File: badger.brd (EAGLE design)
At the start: 100 x 80 mm, 6 parts, among them U1 NCP1402

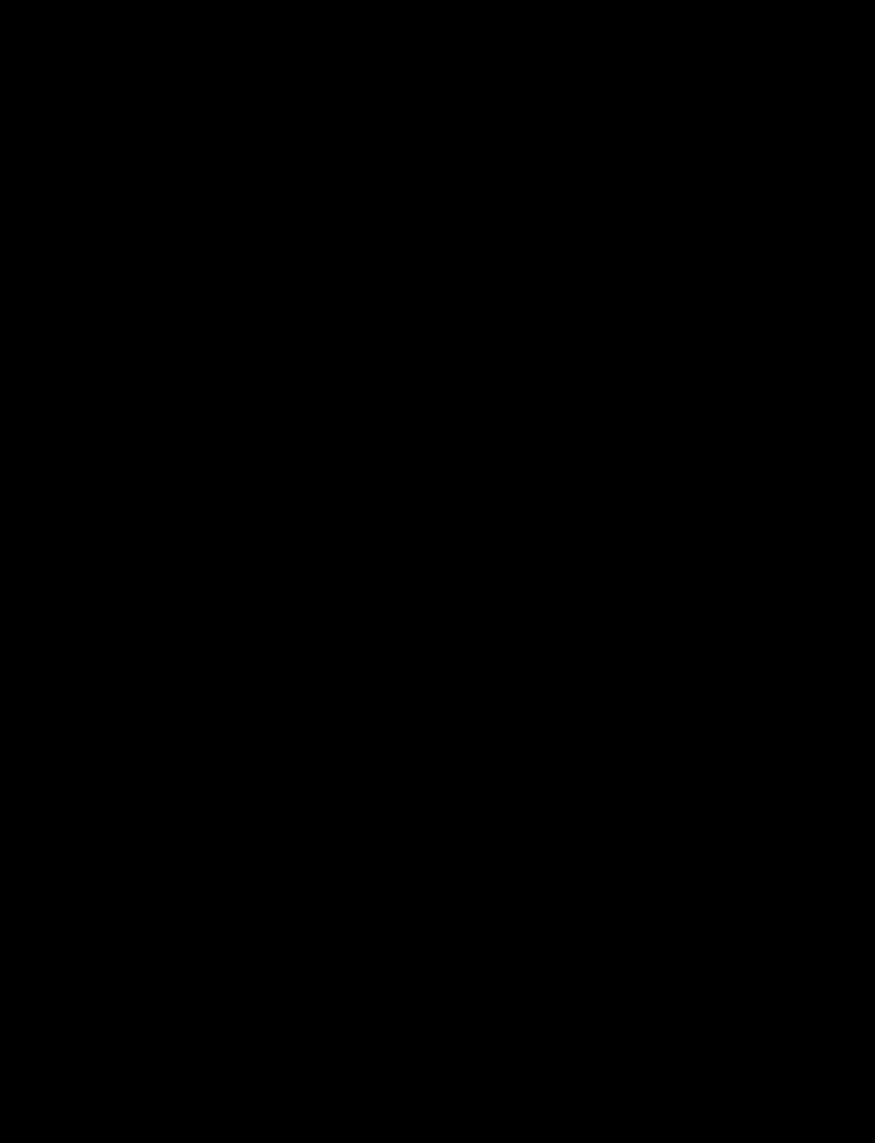
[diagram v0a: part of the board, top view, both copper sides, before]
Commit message: add esp8266 lib and add part
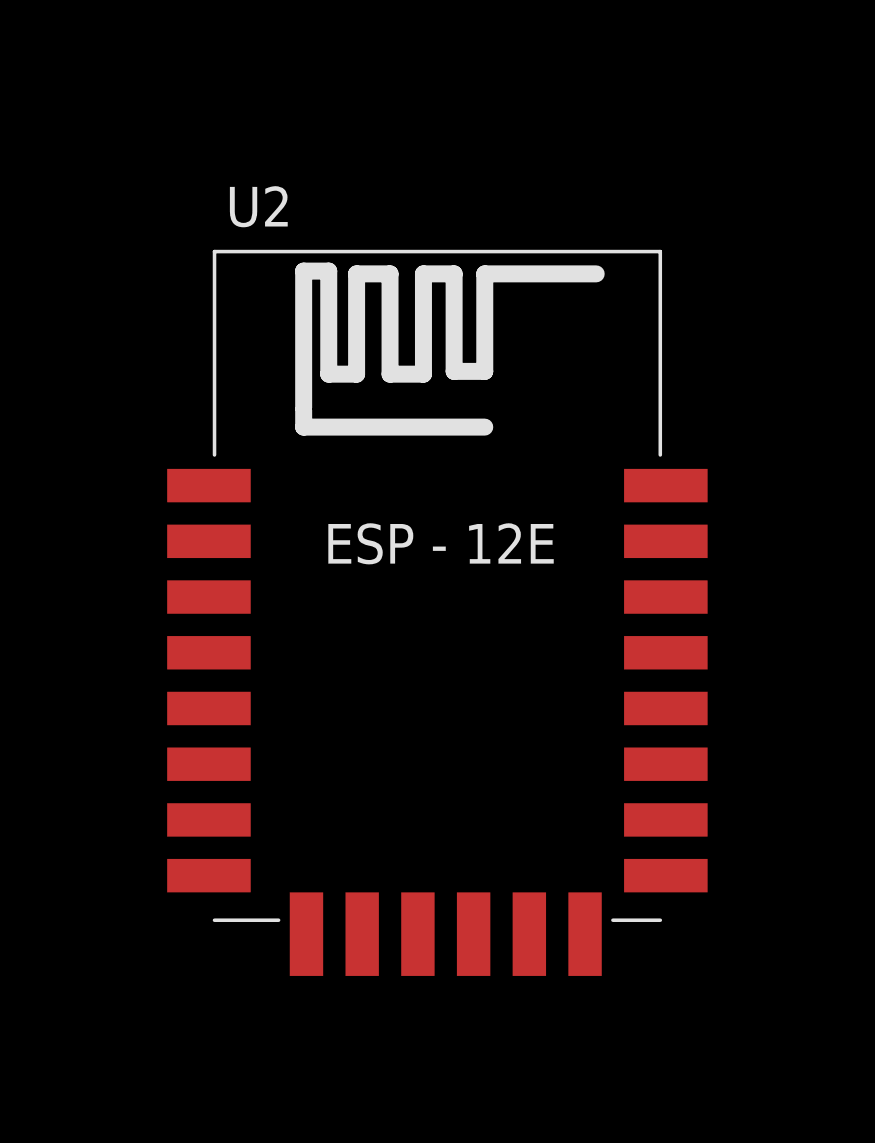
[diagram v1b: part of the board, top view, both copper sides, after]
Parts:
- added U2: (no value), esp8266modules:ESP12E-SMD
- C2: value 68uF -> 100uF
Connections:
- removed net VOUT: C2.A, D1.C, JP1.2, U1.1, U1.2
- new net VCC: C2.A, D1.C, JP1.2, U1.1, U1.2, U2.VCC
- net GND: now also U2.GND
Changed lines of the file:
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@@
 <elements>
 <element name="C1" library="SparkFun" package="EIA3216" value="10uF" x="39.37" y="41.91"/>
-<element name="C2" library="SparkFun" package="EIA3528" value="68uF" x="45.72" y="30.48"/>
+<element name="C2" library="SparkFun" package="EIA3528" value="100uF" x="45.72" y="30.48"/>
 <element name="D1" library="SparkFun" package="SMA-DIODE" value="MBRA140" x="45.72" y="41.91"/>
 <element name="JP1" library="SparkFun" package="1X03" value="" x="41.91" y="35.56"/>
 <element name="L1" library="SparkFun" package="CR54" value="47uH" x="45.72" y="24.13"/>
 <element name="U1" library="SparkFun" package="SOT23-5" value="NCP1402" x="38.1" y="36.83"/>
+<element name="U2" library="esp8266modules" package="ESP12E-SMD" value="" x="68.58" y="30.48"/>
 </elements>
 <signals>
@@
 <wire x1="43.57" y1="41.91" x2="37.15" y2="38.1301" width="0" layer="19" extent="1-1"/>
 </signal>
-<signal name="VOUT">
-<contactref element="U1" pad="1"/>
-<contactref element="U1" pad="2"/>
-<contactref element="D1" pad="C"/>
-<contactref element="C2" pad="A"/>
-<contactref element="JP1" pad="2"/>
-<wire x1="38.1" y1="35.5299" x2="37.15" y2="35.5299" width="0" layer="19" extent="1-1"/>
-<wire x1="44.45" y1="35.56" x2="38.1" y2="35.5299" width="0" layer="19" extent="1-1"/>
-<wire x1="47.37" y1="30.48" x2="44.45" y2="35.56" width="0" layer="19" extent="1-1"/>
-<wire x1="47.87" y1="41.91" x2="44.45" y2="35.56" width="0" layer="19" extent="1-1"/>
-</signal>
 <signal name="GND">
 <contactref element="C2" pad="C"/>
@@
 <contactref element="C1" pad="C"/>
 <contactref element="JP1" pad="1"/>
-<wire x1="41.91" y1="35.56" x2="44.07" y2="30.48" width="0" layer="19" extent="1-1"/>
-<wire x1="39.05" y1="38.1301" x2="41.91" y2="35.56" width="0" layer="19" extent="1-1"/>
+<contactref element="U2" pad="GND"/>
+<wire x1="41.91" y1="35.56" x2="39.05" y2="38.1301" width="0" layer="19" extent="1-1"/>
 <wire x1="37.97" y1="41.91" x2="39.05" y2="38.1301" width="0" layer="19" extent="1-1"/>
+<wire x1="44.07" y1="30.48" x2="41.91" y2="35.56" width="0" layer="19" extent="1-1"/>
+<wire x1="76.68" y1="22.28" x2="44.07" y2="30.48" width="0" layer="19" extent="1-1"/>
 </signal>
 <signal name="VIN">
@@
 <wire x1="40.77" y1="41.91" x2="46.99" y2="35.56" width="0" layer="19" extent="1-1"/>
 </signal>
+<signal name="VCC">
+<contactref element="U1" pad="2"/>
+<contactref element="D1" pad="C"/>
+<contactref element="U1" pad="1"/>
+<contactref element="C2" pad="A"/>
+<contactref element="JP1" pad="2"/>
+<contactref element="U2" pad="VCC"/>
+<wire x1="44.45" y1="35.56" x2="47.87" y2="41.91" width="0" layer="19" extent="1-1"/>
+<wire x1="47.37" y1="30.48" x2="44.45" y2="35.56" width="0" layer="19" extent="1-1"/>
+<wire x1="38.1" y1="35.5299" x2="44.45" y2="35.56" width="0" layer="19" extent="1-1"/>
+<wire x1="37.15" y1="35.5299" x2="38.1" y2="35.5299" width="0" layer="19" extent="1-1"/>
+<wire x1="60.28" y1="22.28" x2="37.15" y2="35.5299" width="0" layer="19" extent="1-1"/>
+</signal>
 </signals>

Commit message: more updates
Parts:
- added GPIO15<->GND, GPIO16<->RESET: SOLDERJUMPERTRACE, SparkFun-Retired:SJ_2S-TRACE
- added JP2, JP3: (no value), SparkFun-Connectors:1X08_ROUND
- added JP4: (no value), SparkFun-Connectors:1X06
- added R1: (no value), SparkFun-Resistors:0603-ARV
- added S1: RESET, SparkFun-Electromechanical:TACTILE-SWITCH-SMD
- added S2: FLASH, SparkFun-Electromechanical:TACTILE-SWITCH-SMD
- added S3: SWITCH-MOMENTARY-2SMD, SparkFun-Electromechanical:TACTILE-SWITCH-SMD
- JP1: device SparkFun:1X03 -> SparkFun-Connectors:1X06_LOCK
- moved JP1 89.2 mm to (2.54, -44.5)
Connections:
- new net 3.3V: C2.A, D1.C, R1.1, R1.5, U1.1, U1.2
- new net ADC: JP2.7, U2.ADC
- new net CH_PD: JP1.5, JP2.6, R1.4, U2.CH_PD
- new net CS0: JP4.1, U2.CS0
- new net GPIO0: JP1.1, JP3.5, R1.8, S2.3, U2.GPIO0
- new net GPIO10: JP4.4, U2.GPIO10
- new net GPIO12: JP2.3, U2.GPIO12
- new net GPIO13: JP2.2, U2.GPIO13
- new net GPIO14: JP2.4, U2.GPIO14
- new net GPIO15: GPIO15<->GND.1, JP3.7, U2.GPIO15
- new net GPIO16: GPIO16<->RESET.2, JP2.5, U2.GPIO16
- new net GPIO2: JP3.6
- new net GPIO4: JP3.3, U2.GPIO4
- new net GPIO5: JP3.4, U2.GPIO5
- new net GPIO9: JP4.3, U2.GPIO9
- new net MISO: JP4.2, U2.MISO
- new net MOSI: JP4.5, U2.MOSI
- new net N$1: U2.GPIO2
- new net N$2: JP1.3
- new net N$4: JP1.2
- new net RESET: GPIO16<->RESET.1, JP2.8, S1.3, U2.RESET
- new net RX: JP3.2, U2.RXD0
- new net SCLK: JP4.6, U2.SCLK
- new net TX: JP3.1, U2.TXD0
- net GND: now also GPIO15<->GND.2, JP3.8, S1.1, S2.1; no longer JP1.1
- net VCC: now also JP1.4, JP2.1; no longer C2.A, D1.C, JP1.2, U1.1, U1.2
- net VIN: no longer JP1.3

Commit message: some updates
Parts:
- removed S3: SWITCH-MOMENTARY-2SMD, SparkFun-Electromechanical:TACTILE-SWITCH-SMD
- added CHEAPO-1, CHEAPO-2, CHEAPO-3: (no value), SparkFun-Retired:SJ_2
- added D2, D3, D4: (no value), SparkFun-LED:LED3MM-NS
- added R2, R3, R4: 100, SparkFun-Resistors:1206
- added R5: 500K, SparkFun-Resistors:0603-RES
- added R6: 250K, SparkFun-Resistors:0603-RES
- added U$1: BATTERY, badger:HOLDER
- moved JP3 146.7 mm to (99.1, 55.9), turned to 270 degrees
- moved JP4 125.0 mm to (78.7, 33.0)
- moved GPIO15<->GND 115.0 mm to (72.4, 30.5)
- moved JP2 112.3 mm to (71.1, 39.4), turned to 90 degrees
- moved JP1 103.4 mm to (94.0, 3.81), turned to 90 degrees
- moved R1 82.1 mm to (72.4, 24.1)
- moved S2 78.2 mm to (69.8, 10.2)
- moved GPIO16<->RESET 74.5 mm to (15.2, 19.1)
- moved S1 65.6 mm to (59.7, 8.89)
- moved U2 26.2 mm to (85.1, 50.8)
- moved L1 24.4 mm to (30.5, 43.2)
- moved C2 18.9 mm to (27.9, 36.8), turned to 270 degrees
- moved D1 14.9 mm to (31.8, 36.8), turned to 270 degrees
- moved C1 2.54 mm to (36.8, 41.9), turned to 180 degrees
- moved U1 1.80 mm to (36.8, 38.1)
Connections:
- new net N$10: CHEAPO-3.2, R4.2
- new net N$11: CHEAPO-1.2, R2.2
- new net N$15: CHEAPO-2.2, R3.2
- new net N$5: D2.A, R2.1
- new net N$6: D3.A, R3.1
- new net N$7: D4.A, R4.1
- net 3.3V: now also R1.3
- net ADC: now also R5.1, R6.2
- net GND: now also D2.K, D3.K, D4.K, R1.7, R6.1, U$1.P$2; no longer GPIO15<->GND.2
- net GPIO12: now also CHEAPO-1.3
- net GPIO13: now also CHEAPO-2.3
- net GPIO15: now also CHEAPO-3.3
- net GPIO2: now also R1.6, U2.GPIO2
- net N$1: now also GPIO15<->GND.2, R1.2; no longer U2.GPIO2
- net VIN: now also CHEAPO-1.1, CHEAPO-2.1, CHEAPO-3.1, R5.2, U$1.P$1

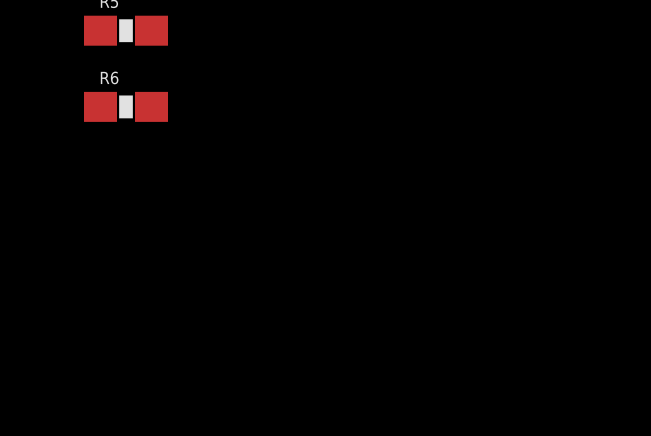
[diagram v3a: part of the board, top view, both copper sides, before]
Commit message: add switch and associated scripting
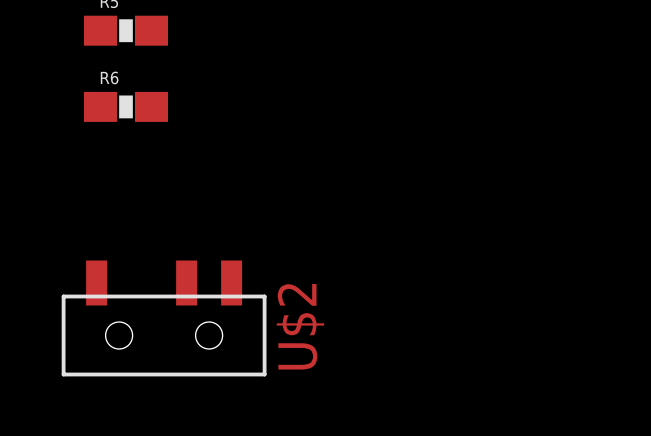
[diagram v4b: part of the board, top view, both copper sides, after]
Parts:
- added U$2: SSSS810701, badger:SSSS8
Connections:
- removed net N$2: JP1.3
- removed net N$4: JP1.2
- removed net VCC: JP1.4, JP2.1, U2.VCC
- new net VFTDI: JP1.4, U$2.P$1
- new net VREG: C2.A, D1.C, U$2.P$3, U1.1, U1.2
- net 3.3V: now also JP2.1, U$2.P$2, U2.VCC; no longer C2.A, D1.C, U1.1, U1.2
- net RX: now also JP1.3
- net TX: now also JP1.2
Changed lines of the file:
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@@
 <element name="R6" library="SparkFun-Resistors" package="0603-RES" value="250K" x="-5.08" y="-106.68"/>
 <element name="U$1" library="badger" package="HOLDER" value="BATTERY" x="10.16" y="49.53"/>
+<element name="U$2" library="badger" package="SSSS8" value="SSSS810701" x="-3.81" y="-114.3"/>
 </elements>
 <signals>
@@
 <wire x1="35.43" y1="41.91" x2="30.48" y2="45.1" width="0" layer="19" extent="1-1"/>
 </signal>
-<signal name="VCC">
-<contactref element="U2" pad="VCC"/>
-<contactref element="JP1" pad="4"/>
-<contactref element="JP2" pad="1"/>
-<wire x1="94.234" y1="11.43" x2="76.79" y2="42.6" width="0" layer="19" extent="1-1"/>
-<wire x1="71.12" y1="39.37" x2="94.234" y2="11.43" width="0" layer="19" extent="1-1"/>
-</signal>
 <signal name="RESET">
 <contactref element="U2" pad="RESET"/>
@@
 <contactref element="U2" pad="RXD0"/>
 <contactref element="JP3" pad="2"/>
-<wire x1="99.06" y1="53.34" x2="93.19" y2="54.6" width="0" layer="19" extent="1-1"/>
+<contactref element="JP1" pad="3"/>
+<wire x1="93.19" y1="54.6" x2="99.06" y2="53.34" width="0" layer="19" extent="1-1"/>
+<wire x1="93.98" y1="8.89" x2="99.06" y2="53.34" width="0" layer="19" extent="1-1"/>
 </signal>
 <signal name="TX">
 <contactref element="U2" pad="TXD0"/>
 <contactref element="JP3" pad="1"/>
-<wire x1="99.06" y1="55.88" x2="93.19" y2="56.6" width="0" layer="19" extent="1-1"/>
+<contactref element="JP1" pad="2"/>
+<wire x1="93.19" y1="56.6" x2="99.06" y2="55.88" width="0" layer="19" extent="1-1"/>
+<wire x1="94.234" y1="6.35" x2="99.06" y2="55.88" width="0" layer="19" extent="1-1"/>
 </signal>
 <signal name="3.3V">
-<contactref element="U1" pad="1"/>
-<contactref element="D1" pad="C"/>
-<contactref element="U1" pad="2"/>
-<contactref element="C2" pad="A"/>
 <contactref element="R1" pad="5"/>
 <contactref element="R1" pad="1"/>
 <contactref element="R1" pad="3"/>
-<wire x1="27.94" y1="35.18" x2="31.75" y2="34.68" width="0" layer="19" extent="1-1"/>
-<wire x1="36.83" y1="36.7999" x2="27.94" y2="35.18" width="0" layer="19" extent="1-1"/>
-<wire x1="35.88" y1="36.7999" x2="36.83" y2="36.7999" width="0" layer="19" extent="1-1"/>
-<wire x1="73.59" y1="24.755" x2="35.88" y2="36.7999" width="0" layer="19" extent="1-1"/>
+<contactref element="U$2" pad="P$2"/>
+<contactref element="JP2" pad="1"/>
+<contactref element="U2" pad="VCC"/>
+<wire x1="71.12" y1="39.37" x2="76.79" y2="42.6" width="0" layer="19" extent="1-1"/>
+<wire x1="73.59" y1="24.755" x2="71.12" y2="39.37" width="0" layer="19" extent="1-1"/>
 <wire x1="72.79" y1="23.505" x2="73.59" y2="24.755" width="0" layer="19" extent="1-1"/>
 <wire x1="71.19" y1="23.505" x2="72.79" y2="23.505" width="0" layer="19" extent="1-1"/>
+<wire x1="-3.06" y1="-112.55" x2="71.19" y2="23.505" width="0" layer="19" extent="1-1"/>
 </signal>
 <signal name="CH_PD">
@@
 <wire x1="71.12" y1="52.07" x2="93.98" y2="13.97" width="0" layer="19" extent="1-1"/>
 </signal>
-<signal name="N$2">
-<contactref element="JP1" pad="3"/>
-</signal>
-<signal name="N$4">
-<contactref element="JP1" pad="2"/>
-</signal>
 <signal name="GPIO16">
 <contactref element="U2" pad="GPIO16"/>
@@
 <wire x1="71.99" y1="23.505" x2="72.898" y2="30.48" width="0" layer="19" extent="1-1"/>
 </signal>
+<signal name="VREG">
+<contactref element="U1" pad="1"/>
+<contactref element="D1" pad="C"/>
+<contactref element="U1" pad="2"/>
+<contactref element="C2" pad="A"/>
+<contactref element="U$2" pad="P$3"/>
+<wire x1="27.94" y1="35.18" x2="-1.56" y2="-112.55" width="0" layer="19" extent="1-1"/>
+<wire x1="31.75" y1="34.68" x2="27.94" y2="35.18" width="0" layer="19" extent="1-1"/>
+<wire x1="35.88" y1="36.7999" x2="31.75" y2="34.68" width="0" layer="19" extent="1-1"/>
+<wire x1="36.83" y1="36.7999" x2="35.88" y2="36.7999" width="0" layer="19" extent="1-1"/>
+</signal>
+<signal name="VFTDI">
+<contactref element="U$2" pad="P$1"/>
+<contactref element="JP1" pad="4"/>
+<wire x1="94.234" y1="11.43" x2="-6.06" y2="-112.55" width="0" layer="19" extent="1-1"/>
+</signal>
 </signals>

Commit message: updates to schematic
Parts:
- removed R2, R3, R4: 100, SparkFun-Resistors:1206
- added CHEAPO-4, CHEAPO-5, CHEAPO-6, CHEAPO-7: (no value), SparkFun-Retired:SJ_2
- added D5: FZR50RGB00T-C, Seeed-OPL-Diode:LED4-1.3-D5.0MM
- added D6: (no value), SparkFun-LED:LED3MM-NS
- added Q1: MOSFET-NCHANNEL2N7002PW, SparkFun-DiscreteSemi:SOT323
- added R10: 100, SparkFun-Resistors:0603-ARV
- added R7, R8, R9: 100, SparkFun-Resistors:1206
- added U$3: PS603SPK, adafruit:PS603
- moved CHEAPO-3 78.1 mm to (-14.0, -168.9)
- moved CHEAPO-2 63.1 mm to (-14.0, -163.8)
- moved CHEAPO-1 63.1 mm to (-14.0, -158.8)
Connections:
- removed net N$10: CHEAPO-3.2, R4.2
- new net N$12: CHEAPO-5.2, R8.1
- new net N$13: CHEAPO-3.2, R10.7
- new net N$14: CHEAPO-2.2, R10.6
- new net N$16: CHEAPO-7.2, R10.8
- new net N$17: CHEAPO-6.2, R9.1
- new net N$18: Q1.2, U$3.1
- new net N$2: D5.R, R8.2
- new net N$4: D5.G, R7.2
- new net N$8: D5.B, R9.2
- new net N$9: CHEAPO-4.2, R7.1
- net 3.3V: now also D5.C
- net GND: now also CHEAPO-4.3, CHEAPO-5.3, CHEAPO-6.3, D6.K, Q1.3
- net GPIO0: now also CHEAPO-7.3
- net GPIO12: now also CHEAPO-4.1; no longer CHEAPO-1.3
- net GPIO13: now also CHEAPO-5.1; no longer CHEAPO-2.3
- net GPIO14: now also CHEAPO-1.3
- net GPIO15: now also CHEAPO-6.1; no longer CHEAPO-3.3
- net GPIO16: now also Q1.1
- net GPIO4: now also CHEAPO-2.3
- net GPIO5: now also CHEAPO-3.3
- net N$11: now also D6.A, R10.1; no longer CHEAPO-1.2, R2.2
- net N$15: now also CHEAPO-1.2, R10.5; no longer CHEAPO-2.2, R3.2
- net N$5: now also R10.2; no longer R2.1
- net N$6: now also R10.3; no longer R3.1
- net N$7: now also R10.4; no longer R4.1
- net VIN: now also CHEAPO-7.1, U$3.2

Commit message: outline, but hit the limits of eagle free
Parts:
- moved CHEAPO-7 220.5 mm to (77.5, 26.7), turned to 90 degrees
- moved Q1 216.4 mm to (76.2, 21.6), turned to 90 degrees
- moved CHEAPO-3 213.8 mm to (72.4, 26.7), turned to 90 degrees
- moved U$3 210.1 mm to (38.1, 19.1), turned to 180 degrees
- moved CHEAPO-2 207.1 mm to (67.3, 26.7), turned to 90 degrees
- moved CHEAPO-1 200.5 mm to (62.2, 26.7), turned to 90 degrees
- moved D5 184.0 mm to (67.3, 54.6)
- moved R10 184.0 mm to (49.5, 26.7), turned to 90 degrees
- moved R7 176.4 mm to (54.6, 44.5)
- moved CHEAPO-4 172.6 mm to (21.6, 38.1)
- moved CHEAPO-5 172.6 mm to (21.6, 33.0)
- moved CHEAPO-6 172.6 mm to (21.6, 27.9)
- moved R8 171.5 mm to (44.5, 39.4)
- moved R5 161.7 mm to (36.8, 52.1)
- moved R6 159.0 mm to (44.5, 44.5)
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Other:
- board size 100 x 80 mm -> 149.2 x 68.3 mm

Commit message: initial placing
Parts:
- added V3.3, VIN, VREG: TEST-POINT3X4, SparkFun-Passives:PAD.03X.04
- moved D2 141.0 mm to (147.0, 47.5), turned to 180 degrees
- moved R9 103.6 mm to (118.1, 62.2), flipped to the bottom, turned to 180 degrees
- moved R8 72.0 mm to (115.6, 50.8), flipped to the bottom, turned to 90 degrees
- moved R7 62.3 mm to (115.6, 57.1), flipped to the bottom, turned to 90 degrees
- moved GPIO16<->RESET 55.9 mm to (58.4, 54.6), flipped to the bottom, turned to 180 degrees
- moved D5 53.4 mm to (120.7, 55.9)
- moved D3 46.9 mm to (53.3, 6.35)
- moved R10 41.9 mm to (91.4, 24.6), flipped to the bottom
- moved Q1 39.0 mm to (39.4, 8.89), flipped to the bottom, turned to 180 degrees
- moved S1 33.7 mm to (61.0, 59.7), flipped to the bottom
- moved S2 33.5 mm to (69.8, 59.7), flipped to the bottom, turned to 180 degrees
- moved JP3 32.4 mm to (106.4, 62.2), turned to 180 degrees
- moved U$2 31.9 mm to (52.1, 62.2), flipped to the bottom, turned to 180 degrees
- moved GPIO15<->GND 31.8 mm to (87.6, 58.4), flipped to the bottom
- moved CHEAPO-1 31.1 mm to (93.2, 29.0), flipped to the bottom
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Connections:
- new net V3.3: V3.3.P$1
- net GPIO4: now also JP3.4; no longer JP3.3
- net GPIO5: now also JP3.3; no longer JP3.4
- net VIN: now also VIN.P$1
- net VREG: now also VREG.P$1
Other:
- board text added: "V3.3"
- board text added: "VIN"
- board text added: "VREG"

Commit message: prior to route
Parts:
- moved D5 13.9 mm to (133.0, 49.6)
- moved U$3 11.2 mm to (27.6, 24.3)
- moved R7 9.71 mm to (124.7, 53.7), turned to 180 degrees
- moved R8 9.21 mm to (124.8, 50.4), turned to 180 degrees
- moved R9 8.24 mm to (124.5, 57.0)
- moved JP1 1.37 mm to (57.3, 50.9)
- moved D1 0.70 mm to (31.2, 57.0)
- moved V3.3 0.14 mm to (20.2, 20.3), flipped to the bottom
- moved VIN 0.14 mm to (20.2, 15.2), flipped to the bottom
- moved VREG 0.14 mm to (20.2, 17.8), flipped to the bottom
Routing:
- added copper zone on layer 16, net GND
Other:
- board text added: "badger badge courtesy of @r00tkillah"
